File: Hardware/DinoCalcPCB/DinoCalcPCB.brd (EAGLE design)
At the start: 106.8 x 73.7 mm, 11 parts, among them J1 AVR_SPI, U1 ATMEGA328P_PDIP

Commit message: Ready to etch for testing
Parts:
- JP2: value (none) -> LEDS
- moved LOGO1 76.7 mm to (6.35, 7.62), turned to 0 degrees
- moved C1 55.1 mm to (63.5, 12.7), turned to 90 degrees
- moved JP1 49.5 mm to (69.8, 15.2), turned to 270 degrees
- moved S1 37.3 mm to (27.9, 19.7), turned to 270 degrees
- moved J1 31.1 mm to (12.7, 50.8)
- moved R1 19.1 mm to (20.3, 27.9)
- moved JP4 8.98 mm to (8.89, 40.6)
- moved JP2 4.58 mm to (33.0, 45.7)
- moved JP3 2.54 mm to (71.1, 27.9)
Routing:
- net N$14: track 21.5 -> 219.6 mm
- net N$10: track 45.7 -> 109.8 mm, vias 0 -> 2
- net VCC: track 170.5 -> 146.9 mm
- net N$9: track 66.1 -> 76.1 mm, vias 0 -> 2
- net N$13: track 89.7 -> 95.7 mm, vias 0 -> 2
- net GND: track 0.65 -> 6.50 mm
- net N$2: track 28.6 -> 22.9 mm
- net N$8: track 23.0 -> 25.5 mm
- net N$7: track 18.6 -> 21.2 mm
- net N$6: track 18.6 -> 21.2 mm
- net N$5: track 23.0 -> 25.5 mm
- net N$4: track 27.3 -> 29.8 mm
- net N$3: track 31.6 -> 33.6 mm
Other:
- board text added: "DINOCALC PCB 1v0 01/2013 JRB"

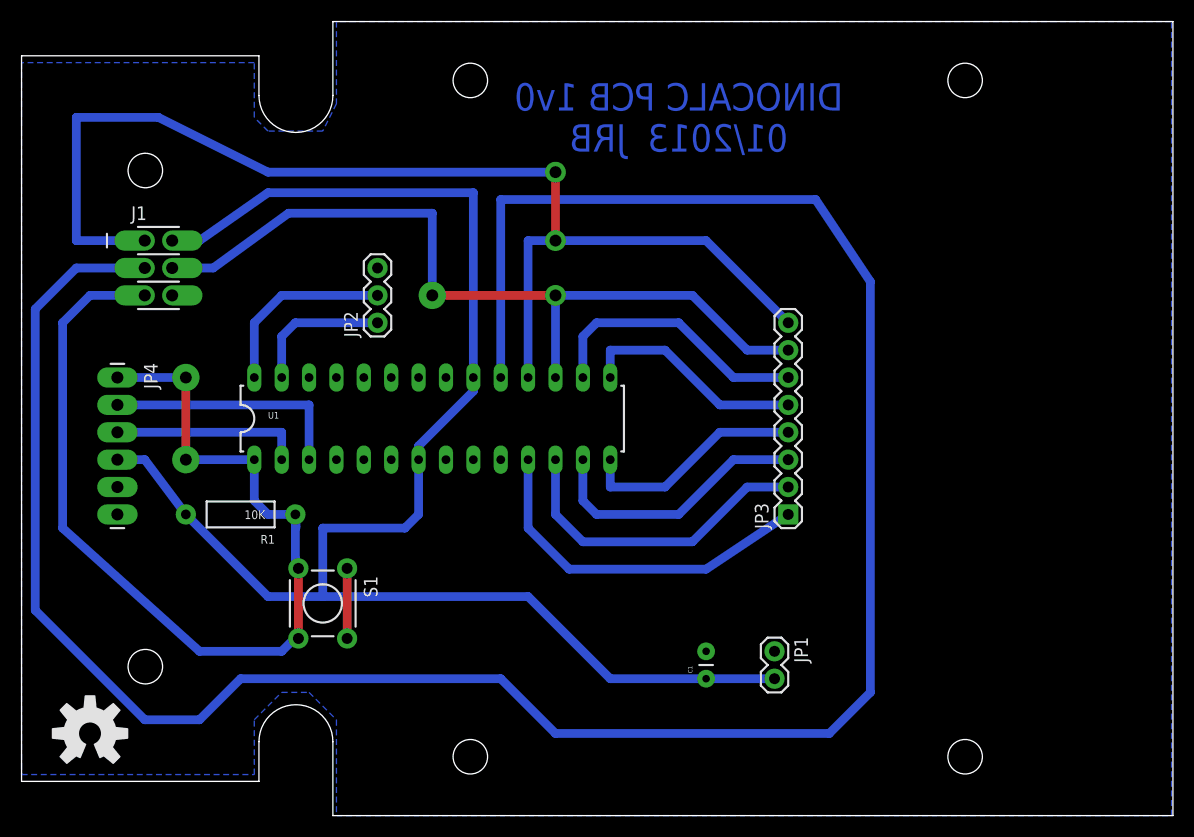
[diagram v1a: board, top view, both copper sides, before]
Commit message: Added diode
Diode added for reverse battery protection.  Also optimized placement of
components a little bit.
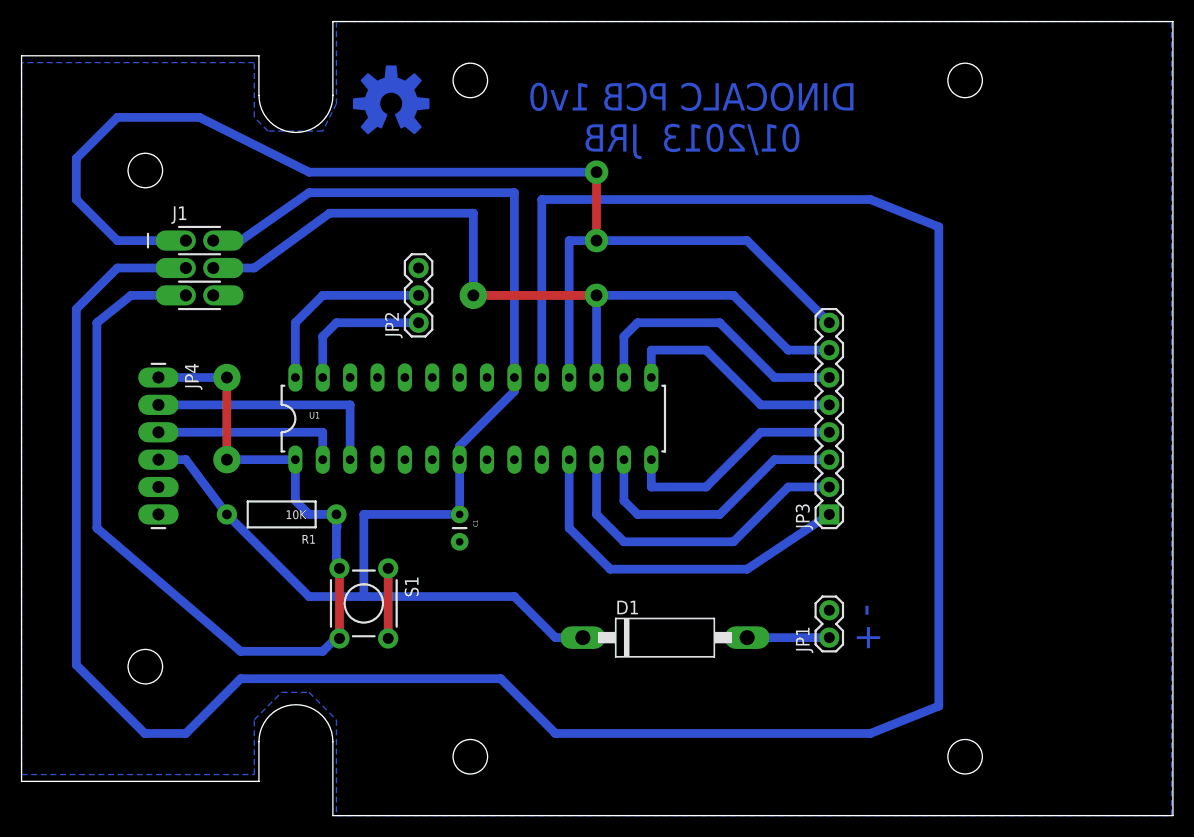
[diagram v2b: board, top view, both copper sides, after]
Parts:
- added D1: 1N5819, adafruit:CB417-15
- moved LOGO1 64.8 mm to (34.3, 66.0)
- moved C1 27.5 mm to (40.6, 27.9), turned to 270 degrees
- moved JP1 5.24 mm to (74.9, 16.5), turned to 90 degrees
- moved J1 3.81 mm to (16.5, 50.8)
- moved JP3 3.81 mm to (74.9, 27.9)
- moved JP4 3.81 mm to (12.7, 40.6)
- moved R1 3.81 mm to (24.1, 27.9)
- moved S1 3.81 mm to (31.8, 19.7)
- moved JP2 3.81 mm to (36.8, 45.7)
- moved U1 3.81 mm to (41.9, 36.8)
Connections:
- new net N$11: D1.A, JP1.1
- net GND: now also JP1.2; no longer JP1.1
- net VCC: now also D1.C; no longer JP1.2
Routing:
- net VCC: track 146.9 -> 124.4 mm
- net N$14: track 219.6 -> 230.4 mm
- net N$11: track 0.00 -> 7.62 mm
- net N$10: track 109.8 -> 112.9 mm
- net N$13: track 95.7 -> 96.6 mm
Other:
- board text added: "+"
- board text added: "-"

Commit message: Updated Version Numbering
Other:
- board text added: "DINOCALC PCB 1v2 01/2013 JRB"
- board text removed: "DINOCALC PCB 1v0 01/2013 JRB"
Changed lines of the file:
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@@
 <hole x="41.6306" y="5.461" drill="3.2"/>
 <hole x="87.5284" y="5.461" drill="3.2"/>
-<text x="62.23" y="64.77" size="2.54" layer="16" font="vector" rot="MR0" align="center">DINOCALC PCB 1v0
+<text x="62.23" y="64.77" size="2.54" layer="16" font="vector" rot="MR0" align="center">DINOCALC PCB 1v2
 01/2013  JRB
 </text>
